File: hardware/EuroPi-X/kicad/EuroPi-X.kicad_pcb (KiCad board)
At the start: 2 copper layers, 86.4 x 110.1 mm, 152 parts, among them J10 Thonkiconn_Mono_Jack, J11 Thonkiconn_Mono_Jack, J12 Thonkiconn_Mono_Jack, J13 Thonkiconn_Mono_Jack, J14 Thonkiconn_Mono_Jack, J15 Thonkiconn_Mono_Jack, J16 Conn_01x30_Pin, J17 Conn_02x08_Odd_Even, J18 Conn_01x16_Pin, J19 Conn_01x16_Pin, J2 Thonkiconn_Mono_Jack, J20 Conn_01x06_Pin, J3 Thonkiconn_Mono_Jack, J4 Conn_01x16_Pin, J5 Thonkiconn_Mono_Jack, J6 Thonkiconn_Mono_Jack, J7 Thonkiconn_Mono_Jack, J8 Thonkiconn_Mono_Jack, J9 Conn_01x16_Pin, P1 Potentiometer_9mm_Vertical_Li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, P2 Potentiometer_9mm_Vertical_Li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, SW2 BOOT, SW3 BOOT, U1 LM4030-4.096, U10 MCP3428, U2 LM4040DBZ-2.0, U3 LM4040DBZ-10, U4 RP2040, U7 TL074, U8 TL074, U9 MCP6004, Y1 Crystal_GND2

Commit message: kicad save
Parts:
- removed J20: Conn_01x06_Pin, Connector_PinHeader_2.54mm:PinHeader_1x06_P2.54mm_Horizontal
- removed TP1, TP2, TP3, TP5: TestPoint, TestPoint:TestPoint_Pad_1.0x1.0mm
- added C35: 100n, Capacitor_SMD:C_0402_1005Metric, F.Cu at (59.4, 60.5)
- added C36: 100n, Capacitor_SMD:C_0402_1005Metric, F.Cu at (59.4, 57.9)
- added JUMPER1: UNI/BIPOLAR, Connector_PinHeader_2.54mm:PinHeader_1x03_P2.54mm_Vertical, B.Cu at (48.3, 73.7)
- added JUMPER3: UNI/BIPOLAR, Connector_PinHeader_2.54mm:PinHeader_1x03_P2.54mm_Vertical, B.Cu at (74.9, 39.4)
- added P1: USB_C_Plug_USB2.0, Connector_USB:USB_C_Receptacle_G-Switch_GT-USB-7010ASV, F.Cu at (66.0, 67.3)
- added R6: 22, Resistor_SMD:R_0402_1005Metric, F.Cu at (54.7, 53.2)
- added R7: 22, Resistor_SMD:R_0402_1005Metric, F.Cu at (51.7, 51.9)
- added U11: L7805, Package_TO_SOT_SMD:TO-252-2, F.Cu at (51.8, 59.2)
- J11: renamed from J17; footprint Eurorack:Eurorack Power Header 16 Pin -> Eurorack:Eurorack Power Header 16 Pin Unlabeled
- TP4: moved to F.Cu
- moved JUMPER2 44.6 mm to (64.0, 39.4)
- moved TP7 43.5 mm to (85.1, 73.7)
- moved TP6 42.0 mm to (80.0, 73.7)
- moved TP8 35.4 mm to (82.5, 73.7)
- moved TP4 23.6 mm to (77.5, 73.7), turned to 0 degrees
- moved C2 14.8 mm to (62.6, 29.8)
- moved R2 11.7 mm to (62.1, 27.9), turned to -90 degrees
- moved C10 11.2 mm to (59.3, 67.8), turned to 90 degrees
- moved C7 10.9 mm to (59.3, 65.3), turned to -90 degrees
- moved C3 8.63 mm to (56.0, 29.8)
- moved Y1 8.15 mm to (54.9, 33.5)
- moved C1 8.13 mm to (49.2, 49.9)
- moved C13 8.13 mm to (48.0, 49.9)
- moved C14 8.13 mm to (59.9, 51.4)
- moved C15 8.13 mm to (46.7, 49.9)
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- renumbered C34 to C28, C28 to C29, C29 to C30, C30 to C31, C31 to C32, C32 to C33, C33 to C34, J9 to J1, J8 to J10, J10 to J12, J11 to J13, J12 to J14, J13 to J15, J14 to J16, J15 to J17, J16 to J18, J18 to J2, J2 to J3, J3 to J4, J4 to J5, J5 to J6, J6 to J7, J19 to J8, J7 to J9, JUMPER1 to JUMPER2, P1 to P2, P2 to P3, R18 to R16, R19 to R17, R20 to R18, R21 to R19, R22 to R20, R23 to R21, R24 to R22, R25 to R23, R26 to R24, R27 to R25, R28 to R26, R29 to R27, R30 to R28, R31 to R29, R32 to R30, R33 to R31, R34 to R32, R37 to R33, R38 to R34, R39 to R35, R40 to R36, R41 to R37, R42 to R38, R43 to R39, R44 to R40, R45 to R41, R46 to R42, R47 to R43, R48 to R44, R49 to R45, R50 to R46, R51 to R47, R52 to R48, R53 to R49, R54 to R50, R55 to R51, R56 to R52, R57 to R53, R58 to R54, R59 to R55, R60 to R56, R61 to R57, SW2 to SW1, SW3 to SW2
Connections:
- TP6 pad 1: /-2.048VREF -> +5V
- TP7 pad 1: /-4.096VREF -> +12V
- TP8 pad 1: /-10VREF -> -12V
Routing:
- net /DAC_OFFSET: track 122.2 -> 74.7 mm, vias 11 -> 6
- net /5VREG_INPUT: track 0.00 -> 44.1 mm, vias 0 -> 5
- net /-4.096VREF: track 68.0 -> 24.6 mm, vias 1 -> 2
- net Earth: track 185.7 -> 224.5 mm, vias 46 -> 50
- net /-2.048VREF: track 62.1 -> 27.1 mm, vias 1 -> 3
- net /RUN: track 70.4 -> 36.7 mm, vias 2 -> 1
- net USB_DP: track 32.0 -> 1.73 mm
- net USB_DN: track 30.9 -> 6.24 mm
- net Net-(P1-D-): track 0.00 -> 23.4 mm
- net Net-(P1-D+): track 0.00 -> 20.9 mm
- net unconnected-(P1-SHIELD-PadS1): track 0.00 -> 19.4 mm
- net +5V: track 109.0 -> 125.5 mm, vias 4 -> 8
- net /BUTTON_2: track 32.8 -> 21.0 mm
- net /BUTTON_1: track 29.9 -> 18.7 mm
- net /-10VREF: track 62.6 -> 73.0 mm, vias 4 -> 8
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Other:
- board size 86.4 x 110.1 mm -> 86.5 x 109.2 mm
- board text added: "+3.3V regulator"
- board text added: "+5v regulator"
- board text added: "b"
- board text added: "bipolar"
- board text added: "cern ohl-s"
- board text added: "e u r o p i x"
- board text added: "eurorack power"
- board text added: "flash"
- board text added: "input adc"
- board text added: "input conditioning"
- board text added: "internal +5V"
- board text added: "output amplification"
- board text added: "output dacs"
- board text added: "r"
- board text added: "red stripe"
- board text added: "rp2040"
- board text added: "unipolar"
- board text added: "usb"
- board text added: "vrefs"
- board text added: "www.allensynthesis.co.uk"
- board text removed: "+3.3V REG"
- board text removed: "-10V"
- board text removed: "-2.048V"
- board text removed: "-4.096V"
- board text removed: "3.3V"
- board text removed: "BIPOLAR ±5V"
- board text removed: "I2C FROM RP2040"
- board text removed: "I2C TO RP2040"
- board text removed: "INPUT ADC"
- board text removed: "INPUT CONDITIONING"
- board text removed: "OUTPUT CONDITIONING"
- board text removed: "OUTPUT DACS"
- board text removed: "UNIPOLAR 0-10V"
- board text removed: "VREF"
- board text removed: "VREFS"
- board text removed: "±10V from jacks"
- board text removed: "±5V OR 0-10V to jacks"

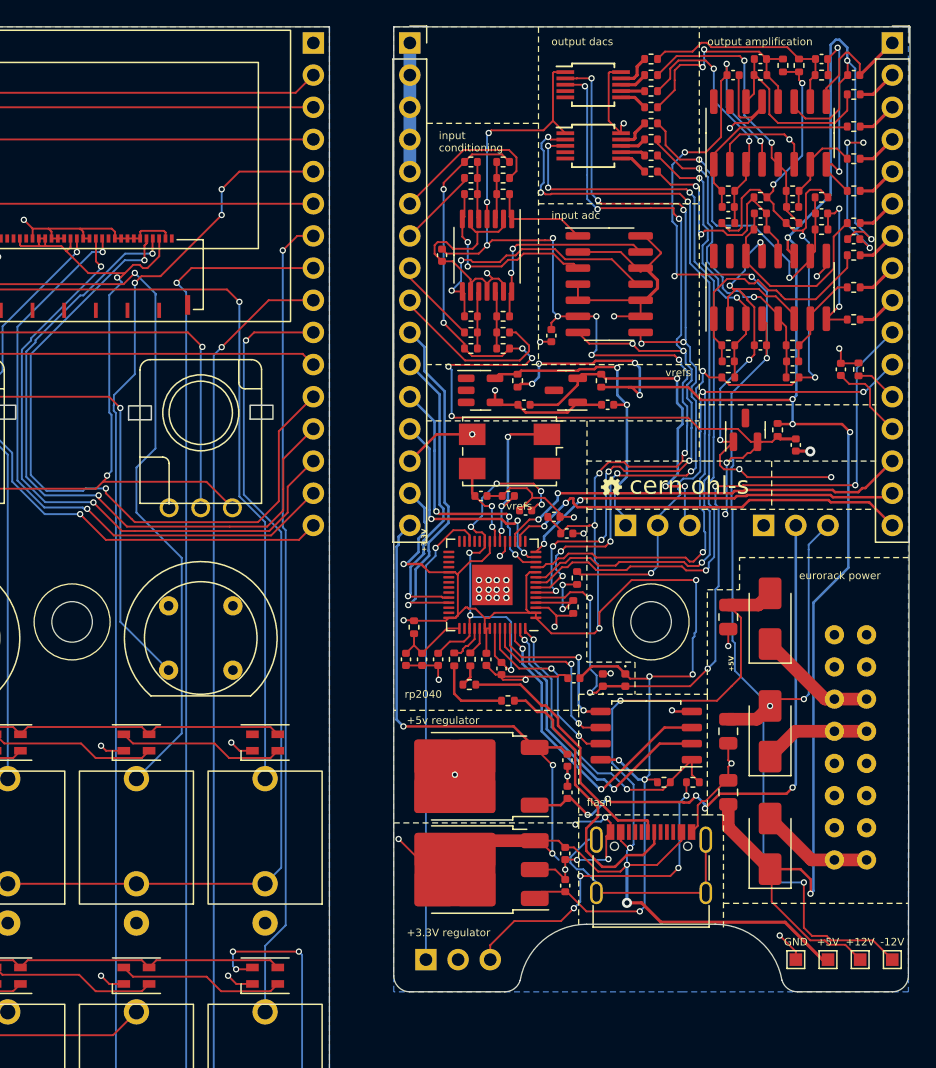
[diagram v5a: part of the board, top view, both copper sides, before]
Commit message: create usb expander
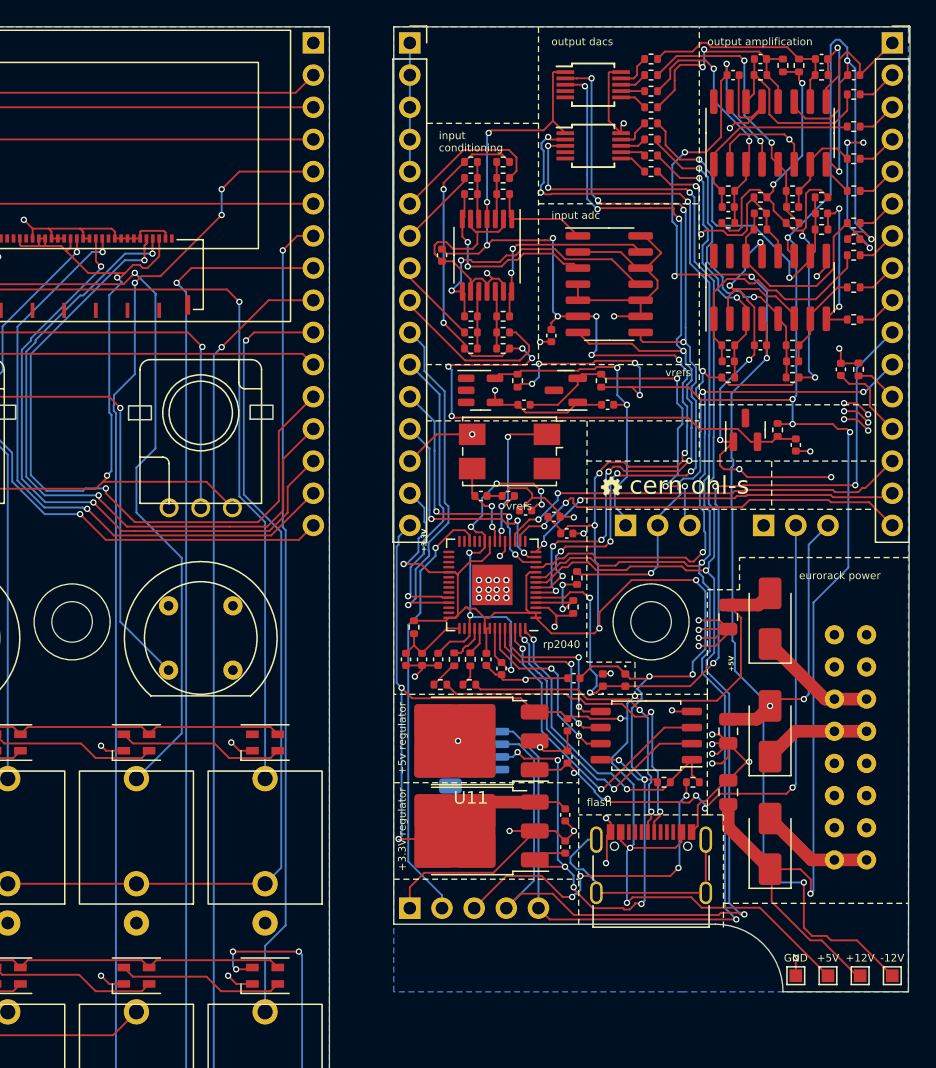
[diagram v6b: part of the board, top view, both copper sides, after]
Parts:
- removed JUMPER1: UNI/BIPOLAR, Connector_PinHeader_2.54mm:PinHeader_1x03_P2.54mm_Vertical
- added J19: Conn_01x05_Pin, Connector_PinHeader_2.54mm:PinHeader_1x05_P2.54mm_Vertical, B.Cu at (47.0, 69.6)
- added J20: Conn_01x04_Pin, Connector_JST:JST_SH_SM04B-SRSS-TB_1x04-1MP_P1.00mm_Horizontal, B.Cu at (52.1, 57.1)
- U11: footprint Package_TO_SOT_SMD:TO-252-2 -> Package_TO_SOT_SMD:TO-252-3_TabPin2
- moved R6 5.48 mm to (49.4, 51.9)
- moved C7 3.05 mm to (59.3, 62.2)
- moved C10 3.05 mm to (59.3, 64.8)
- moved U5 3.05 mm to (51.8, 63.5)
- moved U11 2.79 mm to (51.8, 56.4)
- moved C35 2.79 mm to (59.4, 57.7)
- moved C36 2.79 mm to (59.4, 55.1)
- moved TP4 1.27 mm to (77.5, 74.9)
- moved TP6 1.27 mm to (80.0, 74.9)
- moved TP7 1.27 mm to (85.1, 74.9)
- moved TP8 1.27 mm to (82.5, 74.9)
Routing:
- net /I2C1_SDA: track 61.8 -> 126.9 mm, vias 4 -> 5
- net /I2C1_SCL: track 62.3 -> 124.2 mm, vias 4 -> 5
- net Earth: track 224.5 -> 258.2 mm, vias 50 -> 62
- net IOVDD: track 190.6 -> 208.2 mm, vias 20 -> 23
- net /-10VREF: track 73.0 -> 65.5 mm, vias 8 -> 6
- net +5V: track 125.5 -> 120.8 mm, vias 8 -> 6
- net USB_DN: track 6.24 -> 2.22 mm
- net Net-(P1-D-): track 23.4 -> 27.3 mm, vias 0 -> 2
- net Net-(P1-D+): track 20.9 -> 24.0 mm, vias 0 -> 2
- net /RUN: track 36.7 -> 34.4 mm
- net -12V: track 158.9 -> 159.4 mm
- net +12V: track 124.9 -> 125.4 mm
- net /I2C0_SCL: track 65.8 -> 65.6 mm, vias 10 -> 9
- net /I2C0_SDA: track 70.1 -> 70.0 mm, vias 10 -> 9
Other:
- outline, holes or cut-outs redrawn
- board text added: "expander"
- board text added: "i²c"
- board text removed: "b"
- board text removed: "r"

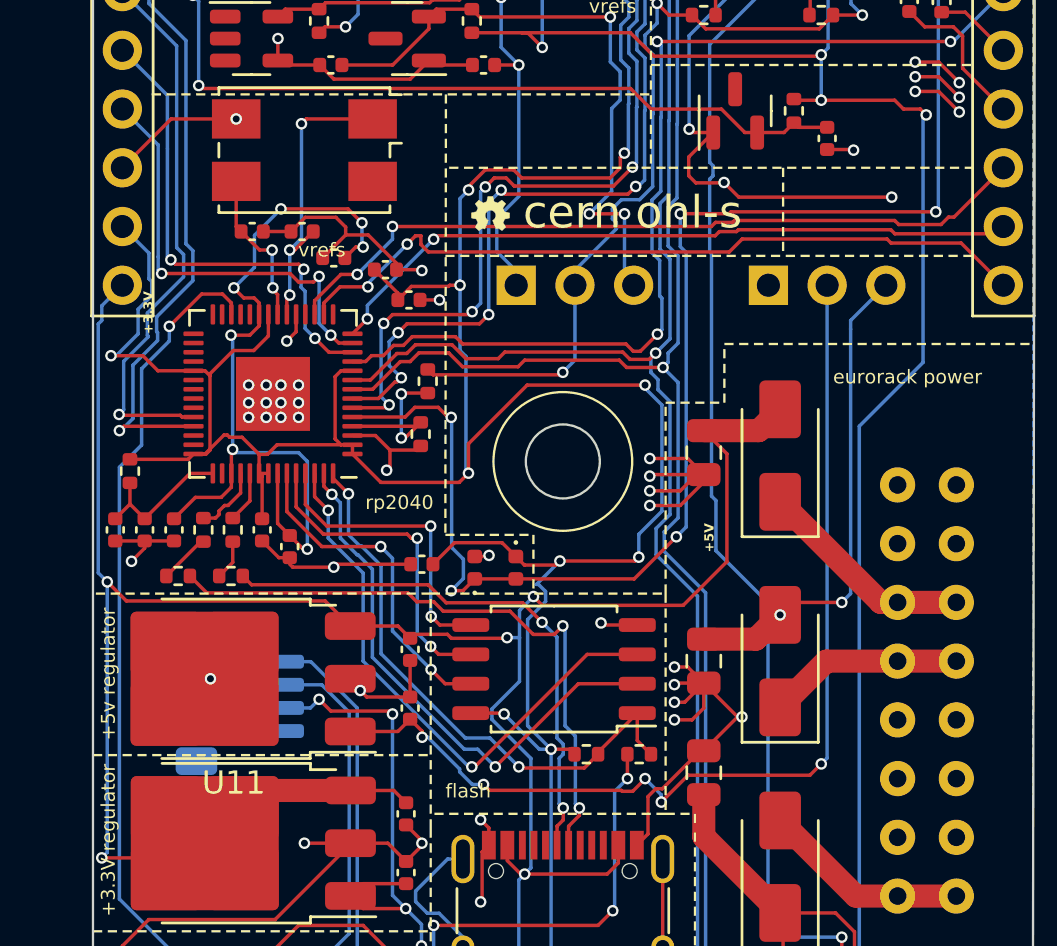
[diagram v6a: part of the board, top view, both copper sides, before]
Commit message: clean up silkscreen
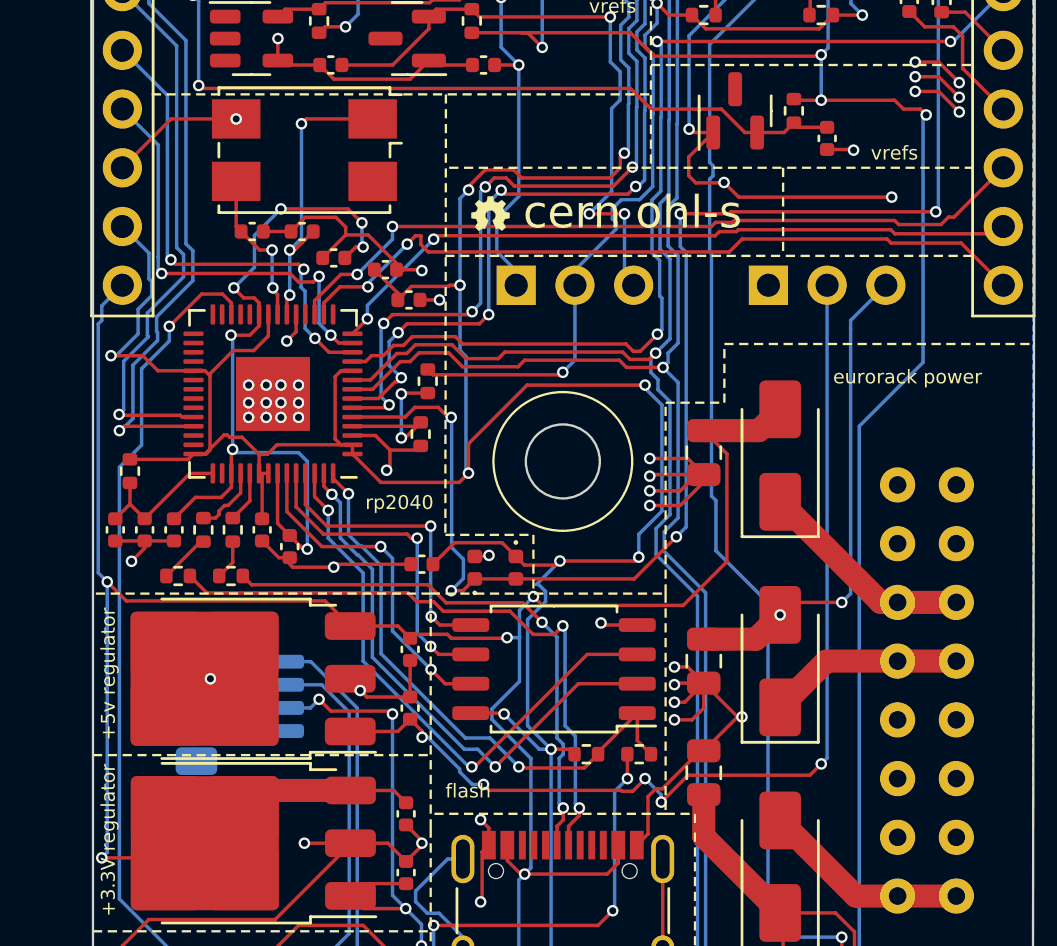
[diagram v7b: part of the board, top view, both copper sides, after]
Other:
- board text removed: "+3.3V"

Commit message: save
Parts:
- moved SW1 1.81 mm to (7.62, 49.0)
- moved SW2 1.81 mm to (27.9, 49.0)
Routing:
- net /BUTTON_1_FRONT: track 24.0 -> 22.2 mm
- net /BUTTON_2_FRONT: track 45.5 -> 44.8 mm
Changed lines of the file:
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@@
   )
   (footprint "Eurorack:Switch Tactile Momentary C&K" (layer "F.Cu")
-    (at 7.62 50.8)
+    (at 7.62 48.990752)
     (property "Sheetfile" "EuroPi-X.kicad_sch")
     (property "Sheetname" "")
@@
   )
   (footprint "Eurorack:Switch Tactile Momentary C&K" (layer "F.Cu")
-    (at 27.94 50.8)
+    (at 27.94 48.990752)
     (property "Sheetfile" "EuroPi-X.kicad_sch")
     (property "Sheetname" "")
@@
   (segment (start 1.27 31.75) (end 5.207 31.75) (width 0.15) (layer "F.Cu") (net 84))
   (via (at 6.223 32.766) (size 0.5) (drill 0.3) (layers "F.Cu" "B.Cu") (net 84))
-  (segment (start 6.223 49.403) (end 7.62 50.8) (width 0.15) (layer "B.Cu") (net 84))
-  (segment (start 6.223 32.766) (end 6.223 49.403) (width 0.15) (layer "B.Cu") (net 84))
+  (segment (start 6.223 32.766) (end 6.223 47.593752) (width 0.15) (layer "B.Cu") (net 84))
+  (segment (start 6.223 47.593752) (end 7.62 48.990752) (width 0.15) (layer "B.Cu") (net 84))
   (segment (start 1.27 29.21) (end 23.241 29.21) (width 0.15) (layer "F.Cu") (net 85))
   (segment (start 23.241 29.21) (end 24.13 30.099) (width 0.15) (layer "F.Cu") (net 85))
   (via (at 24.13 30.099) (size 0.5) (drill 0.3) (layers "F.Cu" "B.Cu") (net 85))
-  (segment (start 24.13 46.99) (end 27.94 50.8) (width 0.15) (layer "B.Cu") (net 85))
+  (segment (start 26.130752 48.990752) (end 27.94 48.990752) (width 0.15) (layer "B.Cu") (net 85))
   (segment (start 24.13 30.099) (end 24.13 46.99) (width 0.15) (layer "B.Cu") (net 85))
+  (segment (start 24.13 46.99) (end 26.130752 48.990752) (width 0.15) (layer "B.Cu") (net 85))
   (segment (start 8.89 26.67) (end 9.906 27.686) (width 0.15) (layer "F.Cu") (net 86))
   (segment (start 1.27 26.67) (end 8.89 26.67) (width 0.15) (layer "F.Cu") (net 86))
